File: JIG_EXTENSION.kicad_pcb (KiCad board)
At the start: 2 copper layers, 180 x 180 mm, 50 parts, among them J1 Conn_01x03_Pin, J10 USB_B, J2 Conn_01x04_Pin, J3 Conn_01x07_Pin, J4 Conn_01x12_Socket, J5 Conn_01x12_Socket, J6 VIN, J7 618037231321, J8 Conn_01x18_Pin, J9 Conn_01x19_Pin, U1 ESP32-DEVKIT-V1, U2 CH340E, U3 AMS1117-3.3, U4 NCP1117DT50RKG, U5 SN74LVC1G3157DBVR

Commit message: ready to produce
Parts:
- removed J2: Conn_01x04_Pin, Connector_JST:JST_XH_S4B-XH-A_1x04_P2.50mm_Horizontal
- removed L1: L, Inductor_SMD:L_0603_1608Metric
- added C10: 100nF, Capacitor_SMD:C_0603_1608Metric, F.Cu at (194.6, 104.3)
- added C11: 18pF, Capacitor_SMD:C_0603_1608Metric, F.Cu at (202.6, 98.3)
- added C12: 1nF, Capacitor_SMD:C_0402_1005Metric, F.Cu at (180.6, 108.9)
- added C13: 100n, Capacitor_SMD:C_0603_1608Metric, F.Cu at (275.2, 44.3)
- added C14: 1u, Capacitor_SMD:C_0603_1608Metric, F.Cu at (272.8, 45.9)
- added C8: 18pF, Capacitor_SMD:C_0603_1608Metric, F.Cu at (199.6, 94.7)
- added C9: 100nF, Capacitor_SMD:C_0603_1608Metric, F.Cu at (204.1, 113.5)
- added D10: LED, LED_SMD:LED_0805_2012Metric, F.Cu at (272.8, 36.9)
- added D11: LED, LED_SMD:LED_0805_2012Metric, F.Cu at (272.8, 32.6)
- added D5: BZX84B4V7LT1, Package_TO_SOT_SMD:SOT-23, F.Cu at (310.7, 34.2)
- added D6: 6.8V CA, Diode_SMD:D_SMB, F.Cu at (245.8, 42.9)
- added D7: 6.8V CA, Diode_SMD:D_SMB, F.Cu at (245.8, 33.9)
- added D8: LED, LED_SMD:LED_0805_2012Metric, F.Cu at (284.8, 45.9)
- added D9: LED, LED_SMD:LED_0805_2012Metric, F.Cu at (295.8, 109.0)
- added J11: VIN, TerminalBlock:TerminalBlock_Altech_AK300-2_P5.00mm, F.Cu at (171.8, 104.5)
- added J12: Conn_01x02_Pin, Connector_PinHeader_2.54mm:PinHeader_1x02_P2.54mm_Horizontal, F.Cu at (175.8, 96.5)
- added J13: Conn_01x02_Pin, Connector_PinHeader_2.54mm:PinHeader_1x02_P2.54mm_Vertical, F.Cu at (219.8, 90.8)
- added J14: Conn_01x02_Pin, Connector_PinHeader_2.54mm:PinHeader_1x02_P2.54mm_Vertical, F.Cu at (219.8, 97.9)
- added J15: Conn_01x02_Pin, Connector_PinHeader_2.54mm:PinHeader_1x02_P2.54mm_Vertical, F.Cu at (219.8, 107.9)
- added J16: Conn_01x02_Pin, Connector_PinHeader_2.54mm:PinHeader_1x02_P2.54mm_Vertical, F.Cu at (219.8, 118.8)
- added J17: VIN, TerminalBlock:TerminalBlock_Altech_AK300-2_P5.00mm, F.Cu at (238.8, 33.9)
- added J18: Conn_01x04_Pin, Connector_PinHeader_2.54mm:PinHeader_1x04_P2.54mm_Horizontal, F.Cu at (228.4, 194.9)
- added J19: Conn_01x04_Pin, Connector_PinHeader_2.54mm:PinHeader_1x04_P2.54mm_Horizontal, F.Cu at (214.6, 194.9)
- added J20: Conn_01x04_Pin, Connector_PinHeader_2.54mm:PinHeader_1x04_P2.54mm_Horizontal, F.Cu at (201.0, 194.8)
- added J21: VIN, TerminalBlock:TerminalBlock_Altech_AK300-2_P5.00mm, F.Cu at (225.8, 33.9)
- added J22: Conn_02x04_Odd_Even, Connector_PinHeader_2.54mm:PinHeader_2x04_P2.54mm_Horizontal, F.Cu at (205.6, 45.4)
- added Q1: WST3325, Package_TO_SOT_SMD:SOT-23, F.Cu at (315.5, 34.4)
- added R23: 100k, Resistor_SMD:R_0603_1608Metric, F.Cu at (311.8, 29.9)
- added R24: 10k, Resistor_SMD:R_0603_1608Metric, F.Cu at (200.6, 114.2)
- added R25: 10k, Resistor_SMD:R_0603_1608Metric, F.Cu at (206.4, 111.1)
- added R26: 0, Resistor_SMD:R_0402_1005Metric, F.Cu at (185.2, 109.9)
- added R27: 0, Resistor_SMD:R_0402_1005Metric, F.Cu at (185.0, 104.7)
- added R28: 2k8, Resistor_SMD:R_0603_1608Metric, F.Cu at (183.2, 108.9)
- added R29: 2k8, Resistor_SMD:R_0603_1608Metric, F.Cu at (183.2, 105.5)
- added R30: DNP, Resistor_SMD:R_0603_1608Metric, F.Cu at (190.0, 107.3)
- added R31: 0, Resistor_SMD:R_0603_1608Metric, F.Cu at (193.8, 110.8)
- added R32: 10k, Resistor_SMD:R_0603_1608Metric, F.Cu at (264.3, 44.5)
- added R33: 10k, Resistor_SMD:R_0603_1608Metric, F.Cu at (267.3, 44.3)
- added R34: 10k, Resistor_SMD:R_0603_1608Metric, F.Cu at (270.8, 44.3)
- added R35: 4k7, Resistor_SMD:R_0603_1608Metric, F.Cu at (258.8, 44.4)
- added R36: 4k7, Resistor_SMD:R_0603_1608Metric, F.Cu at (258.3, 32.9)
- added R37: DNP, Resistor_SMD:R_0603_1608Metric, F.Cu at (255.8, 38.6)
- added R38: 10, Resistor_SMD:R_1206_3216Metric, F.Cu at (251.8, 39.9)
- added R39: 10, Resistor_SMD:R_1206_3216Metric, F.Cu at (251.8, 35.9)
- added R40: DNP, Resistor_SMD:R_0603_1608Metric, F.Cu at (254.3, 44.8)
- added R41: DNP, Resistor_SMD:R_0603_1608Metric, F.Cu at (251.3, 44.8)
- added R42: 0, Resistor_SMD:R_0603_1608Metric, F.Cu at (182.0, 154.9)
- added R43: 0, Resistor_SMD:R_0603_1608Metric, F.Cu at (182.0, 157.9)
- added R44: 0, Resistor_SMD:R_0603_1608Metric, F.Cu at (182.0, 160.9)
- added R45: 2k, Resistor_SMD:R_0603_1608Metric, F.Cu at (284.5, 41.7)
- added R46: 1K, Resistor_SMD:R_0603_1608Metric, F.Cu at (296.6, 113.2)
- added R47: 0, Resistor_SMD:R_0603_1608Metric, F.Cu at (228.8, 185.8)
- added R48: 0, Resistor_SMD:R_0603_1608Metric, F.Cu at (208.8, 185.9)
- added R49: 0, Resistor_SMD:R_0603_1608Metric, F.Cu at (211.8, 185.9)
- added R50: 0, Resistor_SMD:R_0603_1608Metric, F.Cu at (222.8, 185.8)
- added R51: 0, Resistor_SMD:R_0603_1608Metric, F.Cu at (200.8, 176.8)
- added R52: 10K, Resistor_SMD:R_0603_1608Metric, F.Cu at (197.8, 176.9)
- added R53: 1K, Resistor_SMD:R_0603_1608Metric, F.Cu at (269.2, 36.0)
- added R54: 1K, Resistor_SMD:R_0603_1608Metric, F.Cu at (269.2, 33.4)
- added R55: 0, Resistor_SMD:R_0603_1608Metric, F.Cu at (197.0, 115.6)
- added R56: 0, Resistor_SMD:R_0603_1608Metric, F.Cu at (196.8, 101.6)
- added U10: MCP2562-E-MF, Package_DFN_QFN:DFN-8-1EP_3x3mm_P0.65mm_EP1.55x2.4mm, F.Cu at (195.2, 107.1)
- added U11: MAX13487EESAT, footprint:SOIC127P600X175-8N, F.Cu at (261.3, 38.9)
- added U6: SN74LVC1G3157DBVR, Package_TO_SOT_SMD:SOT-23-6, F.Cu at (194.8, 186.1)
- added U9: MCP2515-xST, Package_SO:TSSOP-20_4.4x6.5mm_P0.65mm, F.Cu at (201.6, 107.2)
- added Y1: 16MHz, Crystal:Crystal_SMD_Abracon_ABM8G-4Pin_3.2x2.5mm, F.Cu at (199.7, 98.1)
- D2: value DIODE -> SM712_SOT23; footprint Diode_SMD:D_SOD-323 -> Package_TO_SOT_SMD:SOT-323_SC-70
- J3: footprint Connector_JST:JST_XH_S7B-XH-A_1x07_P2.50mm_Horizontal -> Connector_PinSocket_2.54mm:PinSocket_1x07_P2.54mm_Vertical
- R21, R22: value 470 -> 1K
- moved J6 281.5 mm to (333.1, 41.3), turned to 90 degrees
- moved U4 240.5 mm to (297.7, 37.7), turned to 180 degrees
- moved F2 226.1 mm to (322.4, 34.4), turned to 180 degrees
- moved C5 219.3 mm to (306.5, 33.8), turned to 90 degrees
- moved C6 206.5 mm to (291.8, 33.2), turned to 90 degrees
- moved J1 196.9 mm to (287.4, 68.4), turned to 90 degrees
- moved D1 191.9 mm to (306.8, 46.5), turned to 90 degrees
- moved J3 188.2 mm to (199.8, 62.9)
- moved J7 177.3 mm to (321.4, 168.5), turned to 90 degrees
- moved J4 172.5 mm to (173.4, 134.5), turned to -90 degrees
- moved D2 161.2 mm to (187.2, 107.3)
- moved R1 159.5 mm to (273.5, 84.4)
- moved J5 158.6 mm to (173.4, 173.3), turned to -90 degrees
- moved J10 147.0 mm to (323.9, 114.4), turned to 0 degrees
- moved R2 144.8 mm to (273.0, 80.9)
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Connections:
- net /SPI_INT renamed /CAN_INT
- net Net-(U1-RX2) renamed /UART2_RX
- net Net-(U1-TX2) renamed /UART2_TX
- C5 pad 1: Net-(D2-K) -> Net-(D5-K)
- D2 pad 1: Net-(D2-K) -> Net-(D2-A1)
- D2 pad 2: Net-(D2-A) -> Net-(D2-A2)
- F2 pad 2: Net-(D2-A) -> Net-(Q1-D)
- J4 pad 1: /AGND -> GND
- J5 pad 1: /AGND -> GND
- J5 pad 12: /AGND -> GND
- J7 pad 27: /AGND -> GND
- J7 pad 3: /DB_2 -> /DB_3
- J8 pad 8: /AGND -> GND
- J9 pad 3: /DB_2 -> /DB_3
- R10 pad 2: Net-(D2-K) -> Net-(D5-K)
- R3 pad 2: /UART_RS485_RX -> /UART_RS485_TX
- R4 pad 2: /UART_RS485_TX -> /UART_RS485_RX
- U1 pad 19: unconnected-(U1-D34-Pad19) -> Net-(U1-D34)
- U1 pad 9: unconnected-(U1-D18-Pad9) -> Net-(U1-D18)
- U4 pad 3: Net-(D2-K) -> Net-(D5-K)
- U5 pad 1: unconnected-(U5-B2-Pad1) -> /VCU_SWCLK
- U5 pad 2: unconnected-(U5-GND-Pad2) -> GND
- U5 pad 3: unconnected-(U5-B1-Pad3) -> /SWCLK
- U5 pad 4: unconnected-(U5-A-Pad4) -> /SWCLK_OUT
- U5 pad 5: unconnected-(U5-VCC-Pad5) -> 3V3_B
- U5 pad 6: unconnected-(U5-S-Pad6) -> /SWD_SEL
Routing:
- net 3V3_B: track 0.00 -> 381.7 mm, vias 0 -> 3
- net +12V: track 0.00 -> 322.2 mm
- net 3V3: track 0.00 -> 263.8 mm, vias 0 -> 1
- net /D+/A: track 0.00 -> 191.7 mm, vias 0 -> 1
- net /D-/B: track 0.00 -> 189.2 mm, vias 0 -> 1
- net 5V0: track 0.00 -> 178.2 mm, vias 0 -> 3
- net /DB_11: track 0.00 -> 174.6 mm
- net /DB_12: track 0.00 -> 170.3 mm
- net /UART_RS485_RX: track 0.00 -> 167.7 mm, vias 0 -> 4
- net /DB_13: track 0.00 -> 164.4 mm
- net /DB_14: track 0.00 -> 162.6 mm
- net /UART_RS485_TX: track 0.00 -> 161.8 mm, vias 0 -> 3
- net /DB_1: track 0.00 -> 154.5 mm
- net /DB_2: track 0.00 -> 153.4 mm
- net /DB_5: track 0.00 -> 151.1 mm
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- added copper zone on B.Cu, net GND
- added copper zone on F.Cu, net GND
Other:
- board text added: "12V"
- board text added: "3V3"
- board text added: "3V3 DIO GND CLK"
- board text added: "5V"
- board text added: "CAN BUS"
- board text added: "CAN BUS EXTERNAL"
- board text added: "CAN_H"
- board text added: "CAN_L"
- board text added: "CAN_ROAM_250_H"
- board text added: "CAN_ROAM_250_L"
- board text added: "CAN_ROAM_500_H"
- board text added: "CAN_ROAM_500_L"
- board text added: "D+/A"
- board text added: "D-/B"
- board text added: "DAQ"
- board text added: "DAQ AI0-9"
- board text added: "DAQ AI10-15"
- board text added: "DB37 1 2 3 4 5 6 7 8 9 10 11 12 13 14 15 16 17 18 19"
- board text added: "DB37 20 21 22 23 24 25 26 27"
- board text added: "GND"
- board text added: "GND RXD TXD 3V3"
- board text added: "INT SCK MOSI MISO CS GND 3V3"
- board text added: "NRF SWD"
- board text added: "PSU"
- board text added: "Pin_Description 4V7_BOOST 5V0 UART_TX 60VIN 3V3_ALWAYS_ON UART_RX EBL 4V0_MODEM 3V3_ANT 60V CAN_250_H CAN_250_L CAN_500_H CAN_500_L IM_OUT GPIO_5 GPIO_1 TAMPER_CONN SWDIO"
- board text added: "Pin_Description SWDCLK VCU_SWDIO VCU_SWCLK GPIO_2 GPIO_3 GPIO_4 AIN_100V GND"
- board text added: "RS485"
- board text added: "RS485 EXTERNAL"
- board text added: "RX"
- board text added: "SET D34 LOW TO SELECT NRF"
- board text added: "SWD SELECTOR"
- board text added: "TX"
- board text added: "Test_PIN J7-11 J7-12 J7-13 J7-14 J7-15 J7-16 J7-17 J7-18"
- board text added: "Test_PIN TP1 TP2 TP3 TP4 TP5 TP6 TP7 TP8 TP10 J7-1 J7-2 J7-3 J7-4 J7-5 J7-6 J7-7 J7-8 J7-9 J7-10"
- board text added: "UART2"
- board text added: "UART2 EXTERNAL"
- board text added: "VCU SWD"

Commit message: done
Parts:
- removed C11: 18pF, Capacitor_SMD:C_0603_1608Metric
- removed C12: 1nF, Capacitor_SMD:C_0402_1005Metric
- removed D1, D10: LED, LED_SMD:LED_0805_2012Metric
- removed F2: C1F 2, Fuse:Fuse_1206_3216Metric
- removed J1: Conn_01x03_Pin, Connector_JST:JST_XH_S3B-XH-A_1x03_P2.50mm_Horizontal
- removed J10: USB_B, Connector_USB:USB_B_Lumberg_2411_02_Horizontal
- removed J11, J17, J21: VIN, TerminalBlock:TerminalBlock_Altech_AK300-2_P5.00mm
- removed J12: Conn_01x02_Pin, Connector_PinHeader_2.54mm:PinHeader_1x02_P2.54mm_Horizontal
- removed J13, J14, J15, J16: Conn_01x02_Pin, Connector_PinHeader_2.54mm:PinHeader_1x02_P2.54mm_Vertical
- removed J18, J19, J20: Conn_01x04_Pin, Connector_PinHeader_2.54mm:PinHeader_1x04_P2.54mm_Horizontal
- removed J22: Conn_02x04_Odd_Even, Connector_PinHeader_2.54mm:PinHeader_2x04_P2.54mm_Horizontal
- removed J3: Conn_01x07_Pin, Connector_PinSocket_2.54mm:PinSocket_1x07_P2.54mm_Vertical
- removed J5: Conn_01x12_Socket, Connector_JST:JST_XH_S12B-XH-A-1_1x12_P2.50mm_Horizontal
- removed J8: Conn_01x18_Pin, Connector_PinHeader_2.54mm:PinHeader_1x18_P2.54mm_Vertical
- removed J9: Conn_01x19_Pin, Connector_PinHeader_2.54mm:PinHeader_1x19_P2.54mm_Vertical
- removed Q1: WST3325, Package_TO_SOT_SMD:SOT-23
- removed R21, R22, R53, R54: 1K, Resistor_SMD:R_0603_1608Metric
- removed R23: 100k, Resistor_SMD:R_0603_1608Metric
- removed R24, R25, R34: 10k, Resistor_SMD:R_0603_1608Metric
- removed R26, R27: 0, Resistor_SMD:R_0402_1005Metric
- removed R28, R29: 2k8, Resistor_SMD:R_0603_1608Metric
- removed R30: DNP, Resistor_SMD:R_0603_1608Metric
- removed R31, R48, R49, R50, R51, R55, R56: 0, Resistor_SMD:R_0603_1608Metric
- removed R35, R36: 4k7, Resistor_SMD:R_0603_1608Metric
- removed R45: 2k, Resistor_SMD:R_0603_1608Metric
- removed R52: 10K, Resistor_SMD:R_0603_1608Metric
- removed U10: MCP2562-E-MF, Package_DFN_QFN:DFN-8-1EP_3x3mm_P0.65mm_EP1.55x2.4mm
- removed U4: NCP1117DT50RKG, Package_TO_SOT_SMD:TO-252-2
- removed U6: SN74LVC1G3157DBVR, Package_TO_SOT_SMD:SOT-23-6
- removed U9: MCP2515-xST, Package_SO:TSSOP-20_4.4x6.5mm_P0.65mm
- removed Y1: 16MHz, Crystal:Crystal_SMD_Abracon_ABM8G-4Pin_3.2x2.5mm
- added 3V3_ESP1: TP_V, TestPoint:TestPoint_Pad_D1.0mm, F.Cu at (245.6, 184.9)
- added 3V3_USB1: TP_V, TestPoint:TestPoint_Pad_D1.0mm, F.Cu at (241.0, 182.7)
- added 5V0: TP_V, TestPoint:TestPoint_Pad_D1.0mm, F.Cu at (244.6, 179.9)
- added C15: 10uF, Capacitor_SMD:C_0603_1608Metric, F.Cu at (227.1, 186.9)
- added C16: 100nF, Capacitor_SMD:C_0603_1608Metric, F.Cu at (215.4, 179.5)
- added C17: 1uF, Capacitor_SMD:C_0603_1608Metric, F.Cu at (215.4, 177.9)
- added D12: PESD8V0L2BT-N, Package_TO_SOT_SMD:SOT-23, F.Cu at (226.4, 183.8)
- added D13: SM712_SOT23, Package_TO_SOT_SMD:SOT-323_SC-70, F.Cu at (206.6, 222.1)
- added D14: SM712_SOT23, Package_TO_SOT_SMD:SOT-323_SC-70, F.Cu at (201.2, 225.9)
- added G***: LOGO, LOGO, F.Cu at (240.0, 205.9)
- added GND1: TP_V, TestPoint:TestPoint_Pad_D1.0mm, F.Cu at (249.8, 181.3)
- added IC1: MAX13487EESA+T, YZ-ICs:SOIC127P600X175-8N, F.Cu at (213.5, 183.6)
- added J2: Conn_01x10_Pin, Connector_PinHeader_2.54mm:PinHeader_1x10_P2.54mm_Horizontal, F.Cu at (248.0, 230.3)
- added R57: 10K, Resistor_SMD:R_0603_1608Metric, F.Cu at (209.1, 178.8)
- added R58: 10K, Resistor_SMD:R_0603_1608Metric, F.Cu at (210.7, 178.8)
- added R61: DNP, Resistor_SMD:R_0402_1005Metric, F.Cu at (218.4, 183.7)
- added R63: 10, Resistor_SMD:R_0603_1608Metric, F.Cu at (222.2, 184.7)
- added R64: 10, Resistor_SMD:R_0603_1608Metric, F.Cu at (222.2, 182.7)
- added TP1: rs485_tx, TestPoint:TestPoint_Pad_D1.0mm, F.Cu at (208.6, 181.7)
- added TP2: rs485_tx, TestPoint:TestPoint_Pad_D1.0mm, F.Cu at (208.8, 185.9)
- added U12: K10-3U8S16D, YZ-Connector:K10-3U8S16D, F.Cu at (232.2, 219.9)
- added U8: ESP32-S3-WROOM-1_Devkit, YZ-Connector:ESP32S3_DevkitPinHeader_1x22_P2.54mm_Vertical, F.Cu at (218.3, 192.0)
- C1, C13, C4: value 100n -> 100nF
- C14: value 1u -> 100nF
- C2, C3: value 1u -> 1uF
- C5: value 10uF -> 0.33uF; footprint Capacitor_SMD:C_1206_3216Metric -> Capacitor_SMD:C_0805_2012Metric
- C6: value 10uF -> 100nF
- C8: value 18pF -> 10uF
- D11: value LED -> SS14; footprint LED_SMD:LED_0805_2012Metric -> Diode_SMD:D_SMA
- D2: value SM712_SOT23 -> 3V3_Z; footprint Package_TO_SOT_SMD:SOT-323_SC-70 -> Diode_SMD:D_SOD-323
- D3, D4, D8, D9: footprint LED_SMD:LED_0805_2012Metric -> LED_SMD:LED_0603_1608Metric
- D5: value BZX84B4V7LT1 -> SS14; footprint Package_TO_SOT_SMD:SOT-23 -> Diode_SMD:D_SMA
- D6: value 6.8V CA -> SM712_SOT23; footprint Diode_SMD:D_SMB -> Package_TO_SOT_SMD:SOT-323_SC-70
- D7: value 6.8V CA -> 3V3_Z; footprint Diode_SMD:D_SMB -> Diode_SMD:D_SOD-323
- J4: value Conn_01x12_Socket -> USB_B_Micro; footprint Connector_JST:JST_XH_S12B-XH-A-1_1x12_P2.50mm_Horizontal -> Connector_USB:USB_Micro-B_Molex-105017-0001
- J7: value 618037231321 -> Conn_01x17_Pin; footprint footprint:618037231321 -> Connector_PinHeader_2.54mm:PinHeader_1x17_P2.54mm_Horizontal
- R1, R2: value 0 -> 22; footprint Resistor_SMD:R_0603_1608Metric -> Resistor_SMD:R_0402_1005Metric
- R10: value 5k -> 0
- R3, R4, R5, R7, R8, R9: value 0 -> 4K7
- R32, R33: value 10k -> 22; footprint Resistor_SMD:R_0603_1608Metric -> Resistor_SMD:R_0402_1005Metric
- R37, R40, R41: value DNP -> 0
- R38, R39: value 10 -> 0; footprint Resistor_SMD:R_1206_3216Metric -> Resistor_SMD:R_0603_1608Metric
- R46: value 1K -> 4K7
- U1: value ESP32-DEVKIT-V1 -> USBLC6-2SC6; footprint footprint:MODULE_ESP32_DEVKIT_V1 -> Package_TO_SOT_SMD:SOT-23-6
- U11: value MAX13487EESAT -> TJA1051T/3; footprint footprint:SOIC127P600X175-8N -> Package_SO:SOIC-8_3.9x4.9mm_P1.27mm
- U5: value SN74LVC1G3157DBVR -> L78L05_SOT89; footprint Package_TO_SOT_SMD:SOT-23-6 -> Package_TO_SOT_SMD:SOT-89-3
- moved D5 223.7 mm to (192.2, 223.9), turned to 90 degrees
- moved J6 218.6 mm to (168.8, 185.5)
- moved R10 208.7 mm to (200.4, 221.9)
- moved C6 205.1 mm to (179.5, 204.8), turned to 0 degrees
- moved C5 189.3 mm to (186.2, 179.9), turned to -90 degrees
- moved R39 188.9 mm to (231.8, 223.7), turned to 90 degrees
- moved R37 183.1 mm to (200.7, 213.3), turned to 90 degrees
- moved R38 181.5 mm to (198.1, 213.3), turned to 90 degrees
- moved R40 180.1 mm to (234.0, 223.7), turned to 90 degrees
- moved R41 179.6 mm to (236.0, 223.7), turned to 90 degrees
- moved D7 176.5 mm to (175.2, 195.7), turned to -90 degrees
- moved D11 173.3 mm to (179.6, 178.7), turned to 180 degrees
- moved U11 173.1 mm to (212.7, 205.1)
- moved C13 171.6 mm to (207.8, 202.2), turned to -90 degrees
- moved C1 169.8 mm to (170.8, 207.3), turned to -90 degrees
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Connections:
- C1 pad 1: Net-(J10-VBUS) -> /USB_VBUS
- C10 pad 1: GND -> 5V0
- C10 pad 2: 3V3_B -> GND
- C13 pad 1: 3V3 -> GND
- C13 pad 2: GND -> 3V3_OUT_ESP
- C14 pad 1: 3V3 -> GND
- C14 pad 2: GND -> 5V0
- C2 pad 1: Net-(J10-VBUS) -> /USB_VBUS
- C5 pad 1: Net-(D5-K) -> 12V
- C6 pad 1: 5V0 -> 3V3_B
- C8 pad 1: /CAN_OSC_1 -> 3V3_B
- C9 pad 1: GND -> 12V
- C9 pad 2: 3V3_B -> GND
- D11 pad 1: Net-(D11-K) -> 12V
- D11 pad 2: 3V3 -> Net-(D11-A)
- D2 pad 1: Net-(D2-A1) -> /IGN
- D2 pad 2: Net-(D2-A2) -> GND
- D5 pad 1: Net-(D5-A) -> /VBAT
- D5 pad 2: (no net) -> 3V3_B
- D6 pad 1: /D+/A -> /CAN_500_H
- D6 pad 2: GND -> /CAN_500_L
- D7 pad 1: /D-/B -> /IM
- J4 pad 1: GND -> /USB_VBUS
- J4 pad 2: /AI10 -> Net-(J4-D-)
- J4 pad 3: /AI11 -> Net-(J4-D+)
- J4 pad 4: /AI12 -> unconnected-(J4-ID-Pad4)
- J4 pad 5: /AI13 -> GND
- J4 pad 6: /AI14 -> GND
- J6 pad 2: +12V -> Net-(D11-A)
- J7 pad 1: /DB_1 -> /RXD0
- J7 pad 10: /DB_10 -> /D-
- J7 pad 11: /DB_11 -> /D+
- J7 pad 12: /DB_12 -> /C_H
- J7 pad 13: /DB_13 -> /C_L
- J7 pad 14: /DB_14 -> /IO_E
- J7 pad 15: /DB_15 -> /ADC_I
- J7 pad 16: /DB_16 -> GND
- J7 pad 17: /DB_17 -> 12V
- J7 pad 2: /DB_2 -> /TXD0
- J7 pad 3: /DB_3 -> /EN
- J7 pad 4: /DB_4 -> /IO0
- J7 pad 5: /DB_5 -> /NTC
- J7 pad 6: /DB_6 -> /VBAT
- J7 pad 7: /DB_7 -> GND
- J7 pad 8: /DB_8 -> /IGN
- J7 pad 9: /DB_9 -> /IM
- R1 pad 1: Net-(U1-D22) -> Net-(R1-Pad1)
- R1 pad 2: /UART_QT_RX -> Net-(J4-D+)
- R10 pad 1: Net-(D1-A) -> /IO0
- R10 pad 2: Net-(D5-K) -> Net-(U8-IO5)
- R11 pad 1: /AI0 -> /D-
- R11 pad 2: /DB_1 -> /D-/B
- R12 pad 1: /AI1 -> /D+
- R12 pad 2: /DB_2 -> /D+/A
- R13 pad 1: /AI2 -> /C_H
- R13 pad 2: /DB_5 -> /CAN_500_H
- R14 pad 1: /AI3 -> /C_L
- R14 pad 2: /DB_7 -> /CAN_500_L
- R15 pad 1: /AI4 -> /RS485_TX
- R15 pad 2: /DB_8 -> Net-(R15-Pad2)
- R16 pad 1: /AI5 -> /RS485_RX
- R16 pad 2: /DB_9 -> Net-(U8-IO16)
- R17 pad 1: Net-(J10-D+) -> /K10_TX
- R17 pad 2: Net-(U2-UD+) -> Net-(U8-IO17)
- R18 pad 1: Net-(J10-D-) -> /K10_RX
- R18 pad 2: Net-(U2-UD-) -> Net-(U8-IO18)
- R19 pad 1: Net-(U2-TXD) -> /RXD0
- R19 pad 2: /UART_QT_RX -> /CH340_TX
- R2 pad 1: Net-(U1-D23) -> Net-(R2-Pad1)
- R2 pad 2: /UART_QT_TX -> Net-(J4-D-)
- R20 pad 1: Net-(U2-RXD) -> /TXD0
- R20 pad 2: /UART_QT_TX -> /CH340_RX
- R3 pad 1: /UART2_RX -> /CH340_TX
- R3 pad 2: /UART_RS485_TX -> Net-(D3-K)
- R32 pad 1: /UART_RS485_TX -> Net-(IC1-RO)
- R32 pad 2: 3V3 -> /RS485_RX
- R33 pad 1: Net-(U11-~{RE}) -> Net-(IC1-DI)
- R33 pad 2: 3V3 -> /RS485_TX
- R37 pad 1: Net-(U11-B) -> Net-(U8-IO40)
- R37 pad 2: Net-(U11-A) -> /CAN_TXD
- R38 pad 1: /D+/A -> Net-(U8-IO39)
- R38 pad 2: Net-(U11-A) -> /CAN_RXD
- R39 pad 1: /D-/B -> /5V0_BUCK
- R39 pad 2: Net-(U11-B) -> Net-(U12-AIN1)
- R4 pad 1: /UART2_TX -> /CH340_RX
- R4 pad 2: /UART_RS485_RX -> Net-(D4-K)
- R40 pad 1: Net-(U11-A) -> 5V0
- R40 pad 2: 3V3 -> Net-(U12-AIN2)
- R41 pad 1: Net-(U11-B) -> /3V3_AWS
- R41 pad 2: 3V3 -> Net-(U12-AIN3)
- R42 pad 1: /D+/A -> /4V0
- R42 pad 2: /A/D+ -> Net-(U12-AIN4)
- R43 pad 1: /D-/B -> /3V3_LDO
- R43 pad 2: /B/D- -> Net-(U12-AIN5)
- R44 pad 1: +12V -> /4V7_BOOST
- R44 pad 2: /+VS -> Net-(U12-AIN6)
- R47 pad 1: /DB_20 -> /3V3_ANT
- R47 pad 2: /SWCLK -> Net-(U12-AIN7)
- R5 pad 1: Net-(U1-D27) -> 5V0
- R5 pad 2: /CAN_INT -> Net-(D8-A)
- R6 pad 1: /MISO -> /EN
- R6 pad 2: Net-(U1-D12) -> Net-(U8-IO4)
- R7 pad 1: /MOSI -> Net-(IC1-~{RE})
- R7 pad 2: Net-(U1-D13) -> 5V0
- R8 pad 1: /SCK -> 5V0
- R8 pad 2: Net-(U1-D14) -> Net-(IC1-A)
- R9 pad 1: /CS -> Net-(IC1-B)
- R9 pad 2: Net-(U1-D15) -> GND
- U1 pad 1: 3V3 -> /USB_DP
- U1 pad 3: Net-(U1-D15) -> /USB_DM
- U1 pad 4: unconnected-(U1-D2-Pad4) -> Net-(R2-Pad1)
- U1 pad 5: unconnected-(U1-D4-Pad5) -> /USB_VBUS
- U1 pad 6: /UART2_RX -> Net-(R1-Pad1)
- U11 pad 1: /UART_RS485_TX -> /CAN_TXD
- U11 pad 2: Net-(U11-~{RE}) -> GND
- U11 pad 3: Net-(U11-~{RE}) -> 5V0
- U11 pad 4: /UART_RS485_RX -> /CAN_RXD
- U11 pad 5: GND -> 3V3_OUT_ESP
- U11 pad 6: Net-(U11-A) -> /CAN_500_L
- U11 pad 7: Net-(U11-B) -> /CAN_500_H
- U11 pad 8: 3V3 -> GND
- U2 pad 1: Net-(U2-UD+) -> /USB_DP
- U2 pad 2: Net-(U2-UD-) -> /USB_DM
- U2 pad 8: Net-(U2-TXD) -> /CH340_TX
- U2 pad 9: Net-(U2-RXD) -> /CH340_RX
- U3 pad 3: Net-(J10-VBUS) -> /USB_VBUS
- U5 pad 1: /VCU_SWCLK -> 5V0
- U5 pad 3: /SWCLK -> 12V
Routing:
- net +12V: track 322.2 -> 0.00 mm
- net 3V3: track 263.8 -> 0.00 mm, vias 1 -> 0
- net 3V3_B: track 381.7 -> 131.2 mm, vias 3 -> 4
- net /DB_11: track 174.6 -> 0.00 mm
- net /DB_12: track 170.3 -> 0.00 mm
- net /UART_RS485_RX: track 167.7 -> 0.00 mm, vias 4 -> 0
- net /DB_13: track 164.4 -> 0.00 mm
- net /DB_14: track 162.6 -> 0.00 mm
- net /UART_RS485_TX: track 161.8 -> 0.00 mm, vias 3 -> 0
- net /DB_1: track 154.5 -> 0.00 mm
- net /DB_2: track 153.4 -> 0.00 mm
- net /DB_5: track 151.1 -> 0.00 mm
- net /DB_7: track 150.2 -> 0.00 mm
- net /DB_9: track 150.0 -> 0.00 mm
- net /DB_8: track 149.8 -> 0.00 mm
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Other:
- board size 180 x 180 mm -> 93 x 65 mm
- board text added: "1"
- board text added: "10"
- board text added: "17"
- board text added: "RXD0"
- board text added: "VOLTAGE Probe"
- board text added: "Vin"
- board text removed: "12V"
- board text removed: "3V3"
- board text removed: "3V3 DIO GND CLK"
- board text removed: "5V"
- board text removed: "CAN BUS"
- board text removed: "CAN BUS EXTERNAL"
- board text removed: "CAN_H"
- board text removed: "CAN_L"
- board text removed: "CAN_ROAM_250_H"
- board text removed: "CAN_ROAM_250_L"
- board text removed: "CAN_ROAM_500_H"
- board text removed: "CAN_ROAM_500_L"
- board text removed: "D+/A"
- board text removed: "D-/B"
- board text removed: "DAQ"
- board text removed: "DAQ AI0-9"
- board text removed: "DAQ AI10-15"
- board text removed: "DB37 1 2 3 4 5 6 7 8 9 10 11 12 13 14 15 16 17 18 19"
- board text removed: "DB37 20 21 22 23 24 25 26 27"
- board text removed: "GND RXD TXD 3V3"
- board text removed: "INT SCK MOSI MISO CS GND 3V3"
- board text removed: "NRF SWD"
- board text removed: "PSU"
- board text removed: "Pin_Description 4V7_BOOST 5V0 UART_TX 60VIN 3V3_ALWAYS_ON UART_RX EBL 4V0_MODEM 3V3_ANT 60V CAN_250_H CAN_250_L CAN_500_H CAN_500_L IM_OUT GPIO_5 GPIO_1 TAMPER_CONN SWDIO"
- board text removed: "Pin_Description SWDCLK VCU_SWDIO VCU_SWCLK GPIO_2 GPIO_3 GPIO_4 AIN_100V GND"
- board text removed: "RS485"
- board text removed: "RS485 EXTERNAL"
- board text removed: "RX"
- board text removed: "SET D34 LOW TO SELECT NRF"
- board text removed: "SWD SELECTOR"
- board text removed: "TX"
- board text removed: "Test_PIN J7-11 J7-12 J7-13 J7-14 J7-15 J7-16 J7-17 J7-18"
- board text removed: "Test_PIN TP1 TP2 TP3 TP4 TP5 TP6 TP7 TP8 TP10 J7-1 J7-2 J7-3 J7-4 J7-5 J7-6 J7-7 J7-8 J7-9 J7-10"
- board text removed: "UART2"
- board text removed: "UART2 EXTERNAL"
- board text removed: "VCU SWD"

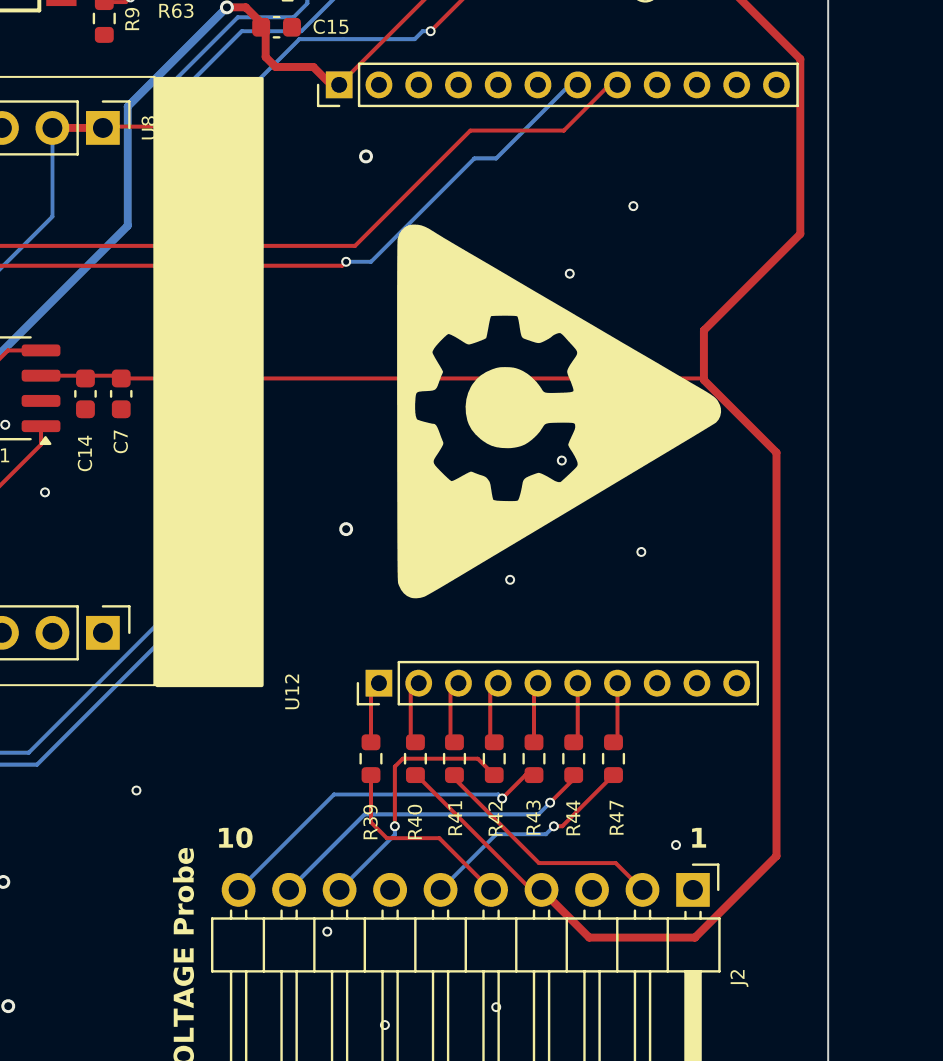
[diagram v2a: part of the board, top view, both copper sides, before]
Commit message: modified 5V0
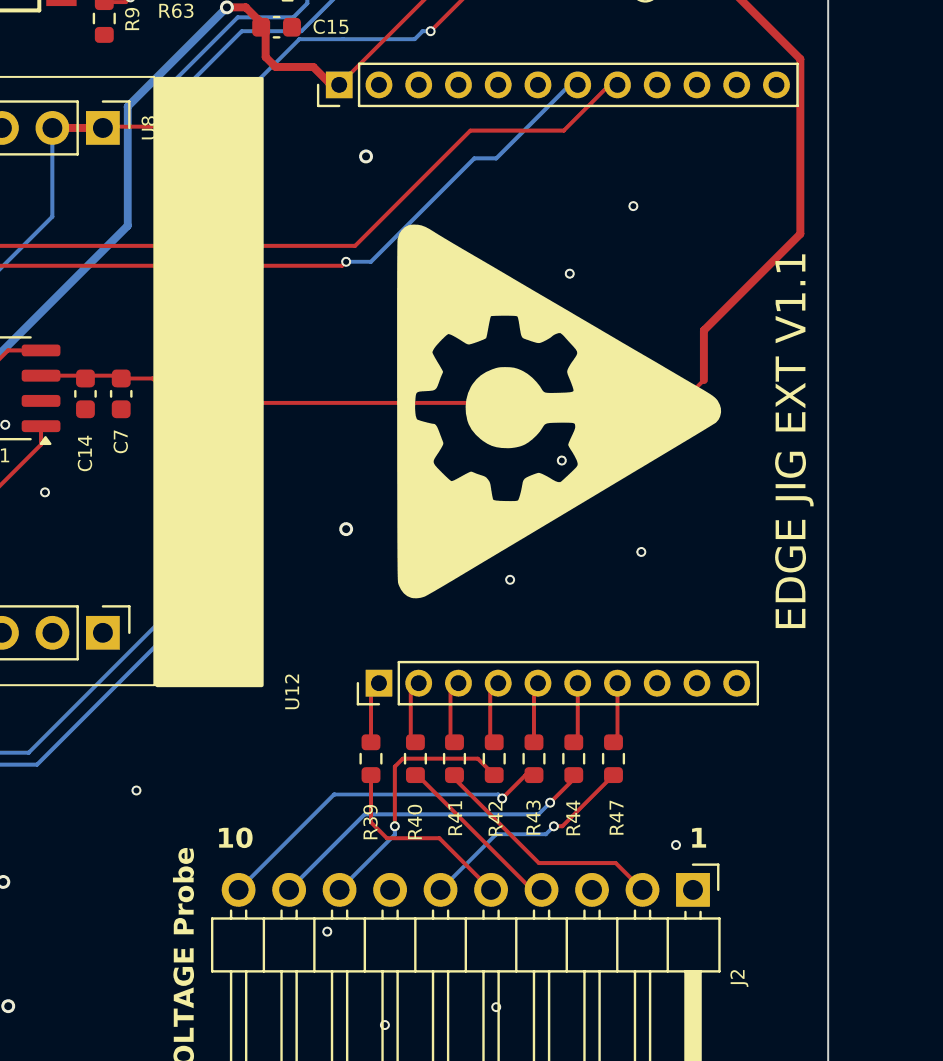
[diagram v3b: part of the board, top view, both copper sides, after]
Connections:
- J2 pad 4: 5V0 -> /5V0_I
- R40 pad 1: 5V0 -> /5V0_I
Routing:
- net 5V0: track 172.6 -> 124.8 mm
- net /5V0_I: track 0.00 -> 8.74 mm
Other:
- board text added: "EDGE JIG EXT V1.1"
